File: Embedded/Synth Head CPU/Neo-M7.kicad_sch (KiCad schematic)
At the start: 1 part, among them U8 NEO-M8M

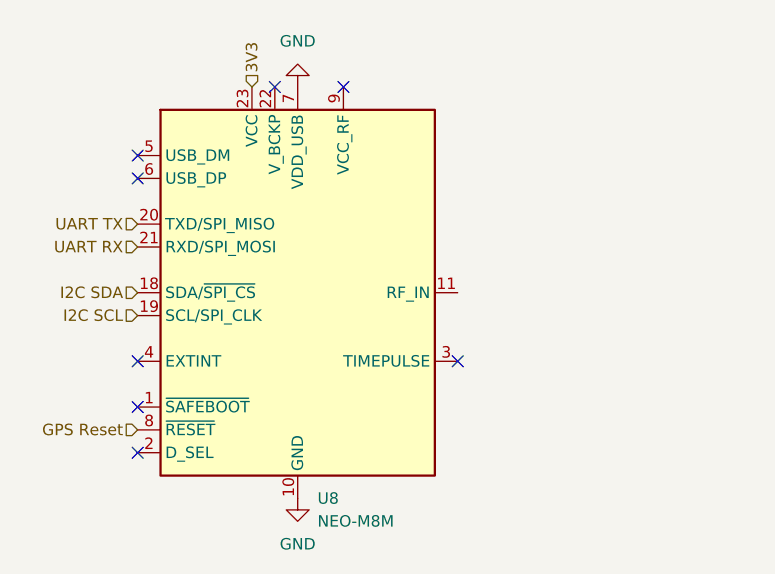
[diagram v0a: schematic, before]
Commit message: Added GPS RF Port
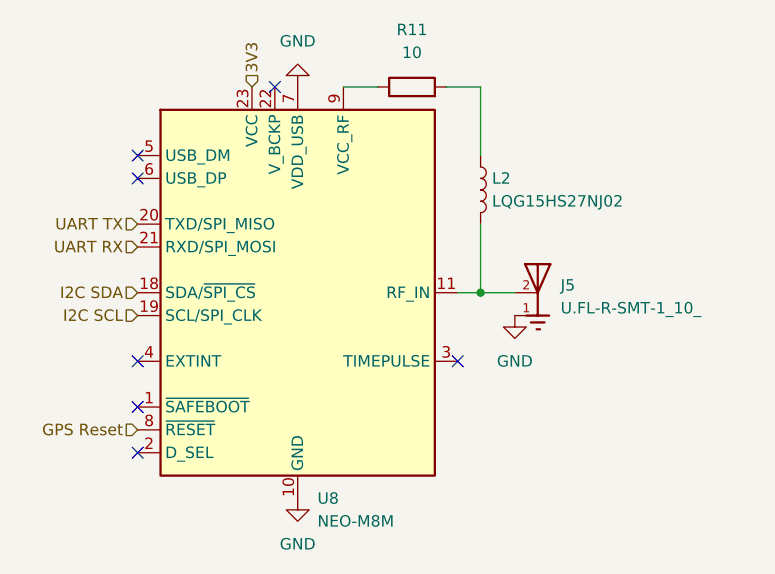
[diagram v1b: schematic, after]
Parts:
- added J5: U.FL-R-SMT-1_10_, U.FL-R-SMT-1_10_:HRS_U.FL-R-SMT-1_10_, symbol RF_Connector_U-FL:U.FL-R-SMT-1_10_
- added L2: LQG15HS27NJ02, symbol Device:L
- added R11: 10, symbol Device:R
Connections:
- net GND: now also J5.1
- net at U8.11 (RF_IN): now also J5.2, L2.2
- net at U8.9 (VCC_RF): now also R11.1
- new net: L2.1, R11.2
- no-connect marks 8 -> 7

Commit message: Prepared All Main Boards for PCB Creation
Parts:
- J5: footprint U.FL-R-SMT-1_10_:HRS_U.FL-R-SMT-1_10_ -> RF_Connector_U-FL:HRS_U.FL-R-SMT-1_10_
- L2: footprint (none) -> Inductor_SMD:L_0402_1005Metric_Pad0.77x0.64mm_HandSolder
- R11: footprint (none) -> Capacitor_SMD:C_0603_1608Metric_Pad1.08x0.95mm_HandSolder
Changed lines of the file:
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@@
 			)
 		)
-		(property "Footprint" ""
+		(property "Footprint" "Capacitor_SMD:C_0603_1608Metric_Pad1.08x0.95mm_HandSolder"
 			(at 154.94 88.138 90)
 			(effects
@@
 			)
 		)
-		(property "Footprint" "U.FL-R-SMT-1_10_:HRS_U.FL-R-SMT-1_10_"
+		(property "Footprint" "RF_Connector_U-FL:HRS_U.FL-R-SMT-1_10_"
 			(at 168.91 109.22 0)
 			(effects
@@
 			)
 		)
-		(property "Footprint" ""
+		(property "Footprint" "Inductor_SMD:L_0402_1005Metric_Pad0.77x0.64mm_HandSolder"
 			(at 162.56 97.79 0)
 			(effects
